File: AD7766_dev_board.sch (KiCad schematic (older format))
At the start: 62 parts, among them J1 Conn_Coaxial, J2 Conn_Coaxial, J3 Conn_01x06_Male, J4 Conn_01x10_Male, U1 PWR_JACK_POS, U2 PWR_JACK_GND, U3 ADR445, U4 ADP3330-5, U5 ADP3330-2.5, U6 ADP3330-2.5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

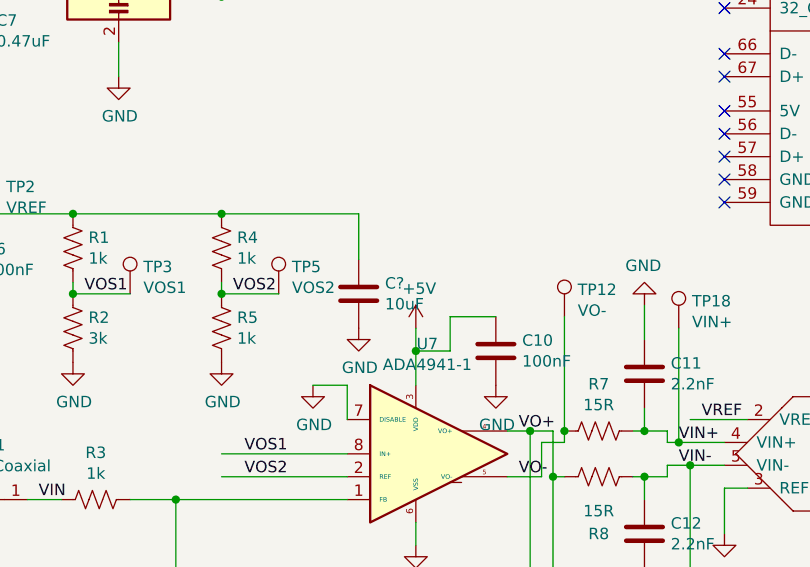
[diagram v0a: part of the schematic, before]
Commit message: revised README, fixed bill of materials
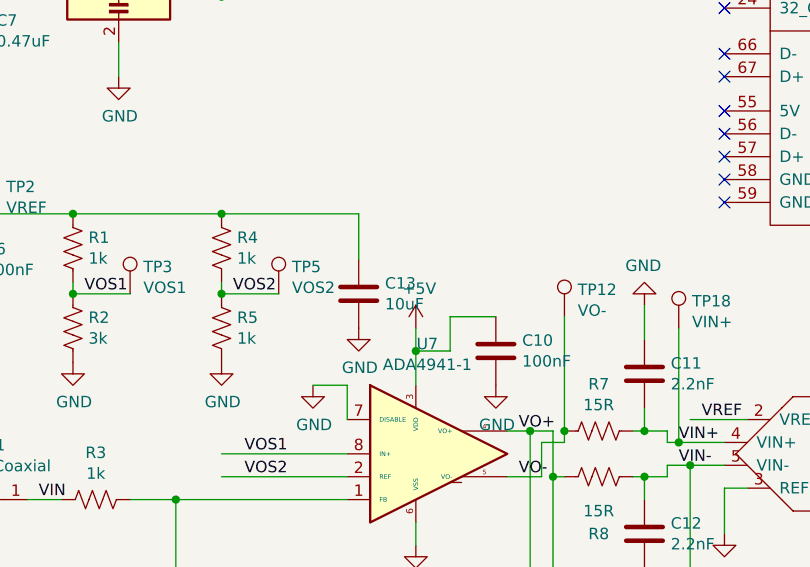
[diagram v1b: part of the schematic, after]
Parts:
- C13: renamed from C?; footprint (none) -> Capacitor_SMD:C_0805_2012Metric_Pad1.15x1.40mm_HandSolder
- D1: footprint Diode_SMD:D_0805_2012Metric_Pad1.15x1.40mm_HandSolder -> Diode_SMD:D_SMA-SMB_Universal_Handsoldering
- D2: Distributor (none) -> Digikey; Distributor Link (none) -> https://www.digikey.com/en/products/detail/nexperia-usa-inc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
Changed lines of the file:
@@
 F 0 "D1" H 2300 5915 50  0000 C CNN
 F 1 "DIODE" H 2300 5824 50  0000 C CNN
-F 2 "Diode_SMD:D_0805_2012Metric_Pad1.15x1.40mm_HandSolder" H 2300 5650 50  0001 C CNN
+F 2 "Diode_SMD:D_SMA-SMB_Universal_Handsoldering" H 2300 5650 50  0001 C CNN
 F 3 "~" H 2300 5650 50  0001 C CNN
 	1    2300 5650
@@
 F 2 "Package_TO_SOT_SMD:SC-59_Handsoldering" H 2850 6250 50  0001 C CNN
 F 3 "~" H 2850 6250 50  0001 C CNN
+F 4 "https://www.digikey.com/en/products/detail/nexperia-usa-inc/PESD15VL2BT215/1157421?s=N4IgTCBcDaIAoFEDKARAjAVgGoBkwCEAVEAXQF8g" H 2850 6250 50  0001 C CNN "Distributor Link"
+F 5 "Digikey" H 2850 6250 50  0001 C CNN "Distributor"
 	1    2850 6250
 	1    0    0    -1
@@
 VIN
 $Comp
-L Device:C C?
+L Device:C C13
 U 1 1 5FFE5A2E
 P 5050 4600
-F 0 "C?" H 5165 4646 50  0000 L CNN
+F 0 "C13" H 5165 4646 50  0000 L CNN
 F 1 "10uF" H 5165 4555 50  0000 L CNN
-F 2 "" H 5088 4450 50  0001 C CNN
+F 2 "Capacitor_SMD:C_0805_2012Metric_Pad1.15x1.40mm_HandSolder" H 5088 4450 50  0001 C CNN
 F 3 "~" H 5050 4600 50  0001 C CNN
 	1    5050 4600
@@
 Connection ~ 4450 4250
 $Comp
-L power:GND #PWR?
+L power:GND #PWR048
 U 1 1 5FFF02BA
 P 5050 4750
-F 0 "#PWR?" H 5050 4500 50  0001 C CNN
+F 0 "#PWR048" H 5050 4500 50  0001 C CNN
 F 1 "GND" H 5055 4577 50  0000 C CNN
 F 2 "" H 5050 4750 50  0001 C CNN

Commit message: updated with errors found in version 1, sending out version 2 for fabrication
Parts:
- removed C13: 10uF, Capacitor_SMD:C_0805_2012Metric_Pad1.15x1.40mm_HandSolder, symbol Device:C
- added H1, H2, H3, H4: MountingHole, my_library_foot:m3_mounting_hole, symbol Mechanical:MountingHole
- R1: value 1k -> 3k
- R2: value 3k -> 1k
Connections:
- wire segments 172 -> 170
- no-connect marks 48 -> 52
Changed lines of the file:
@@
 Wire Wire Line
 	2250 2350 2600 2350
-$Comp
-L power:GND #PWR010
-U 1 1 5F772035
-P 1950 4450
-F 0 "#PWR010" H 1950 4200 50  0001 C CNN
-F 1 "GND" H 1955 4277 50  0000 C CNN
-F 2 "" H 1950 4450 50  0001 C CNN
-F 3 "" H 1950 4450 50  0001 C CNN
-	1    1950 4450
-	1    0    0    -1
-$EndComp
 Wire Wire Line
 	1950 4450 1950 4250
@@
 P 3800 4400
 F 0 "R1" H 3868 4446 50  0000 L CNN
-F 1 "1k" H 3868 4355 50  0000 L CNN
+F 1 "3k" H 3868 4355 50  0000 L CNN
 F 2 "Resistor_SMD:R_0805_2012Metric_Pad1.15x1.40mm_HandSolder" V 3840 4390 50  0001 C CNN
 F 3 "~" H 3800 4400 50  0001 C CNN
@@
 P 3800 4750
 F 0 "R2" H 3868 4796 50  0000 L CNN
-F 1 "3k" H 3868 4705 50  0000 L CNN
+F 1 "1k" H 3868 4705 50  0000 L CNN
 F 2 "Resistor_SMD:R_0805_2012Metric_Pad1.15x1.40mm_HandSolder" V 3840 4740 50  0001 C CNN
 F 3 "~" H 3800 4750 50  0001 C CNN
@@
 Text Label 2850 5800 0    50   ~ 0
 VIN
-$Comp
-L Device:C C13
-U 1 1 5FFE5A2E
-P 5050 4600
-F 0 "C13" H 5165 4646 50  0000 L CNN
-F 1 "10uF" H 5165 4555 50  0000 L CNN
-F 2 "Capacitor_SMD:C_0805_2012Metric_Pad1.15x1.40mm_HandSolder" H 5088 4450 50  0001 C CNN
-F 3 "~" H 5050 4600 50  0001 C CNN
-	1    5050 4600
-	1    0    0    -1
-$EndComp
-Wire Wire Line
-	4450 4250 5050 4250
-Wire Wire Line
-	5050 4250 5050 4450
-Connection ~ 4450 4250
-$Comp
-L power:GND #PWR048
-U 1 1 5FFF02BA
-P 5050 4750
-F 0 "#PWR048" H 5050 4500 50  0001 C CNN
-F 1 "GND" H 5055 4577 50  0000 C CNN
-F 2 "" H 5050 4750 50  0001 C CNN
-F 3 "" H 5050 4750 50  0001 C CNN
-	1    5050 4750
-	1    0    0    -1
-$EndComp
+NoConn ~ 1950 4450
+NoConn ~ 5600 4050
+NoConn ~ 5700 4400
+NoConn ~ 5150 5500
+$Comp
+L Mechanical:MountingHole H1
+U 1 1 5F936B39
+P 1400 6750
+F 0 "H1" H 1500 6796 50  0000 L CNN
+F 1 "MountingHole" H 1500 6705 50  0000 L CNN
+F 2 "my_library_foot:m3_mounting_hole" H 1400 6750 50  0001 C CNN
+F 3 "~" H 1400 6750 50  0001 C CNN
+	1    1400 6750
+	1    0    0    -1
+$EndComp
+$Comp
+L Mechanical:MountingHole H2
+U 1 1 5F9376EF
+P 1450 7000
+F 0 "H2" H 1550 7046 50  0000 L CNN
+F 1 "MountingHole" H 1550 6955 50  0000 L CNN
+F 2 "my_library_foot:m3_mounting_hole" H 1450 7000 50  0001 C CNN
+F 3 "~" H 1450 7000 50  0001 C CNN
+	1    1450 7000
+	1    0    0    -1
+$EndComp
+$Comp
+L Mechanical:MountingHole H3
+U 1 1 5F937926
+P 1450 7200
+F 0 "H3" H 1550 7246 50  0000 L CNN
+F 1 "MountingHole" H 1550 7155 50  0000 L CNN
+F 2 "my_library_foot:m3_mounting_hole" H 1450 7200 50  0001 C CNN
+F 3 "~" H 1450 7200 50  0001 C CNN
+	1    1450 7200
+	1    0    0    -1
+$EndComp
+$Comp
+L Mechanical:MountingHole H4
+U 1 1 5F937B08
+P 2300 7050
+F 0 "H4" H 2400 7096 50  0000 L CNN
+F 1 "MountingHole" H 2400 7005 50  0000 L CNN
+F 2 "my_library_foot:m3_mounting_hole" H 2300 7050 50  0001 C CNN
+F 3 "~" H 2300 7050 50  0001 C CNN
+	1    2300 7050
+	1    0    0    -1
+$EndComp

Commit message: added allPCB BOM and position files. Hopefully it works.
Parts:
- C1: Manufacturer Part # (none) -> GRM21BR6YA106ME43L
- C10, C3, C6, CD1, CD4, CD6: Manufacturer Part # (none) -> C0805C104M5RACTU
- C11, C12: Manufacturer Part # (none) -> CL21B222KDCNFNC
- C2, C4, C5, C7, C8, C9: Manufacturer Part # (none) -> 08051C474K4Z2A
- CD2, CD5, CD8: Manufacturer Part # (none) -> 08055C102KAT2A
- CD3, CD7, CD9: Manufacturer Part # (none) -> C0805C101J5GACTU
- D1: Manufacturer Part # (none) -> SK220ATR
- D2: Manufacturer Part # (none) -> PESD15VL2BT,215
- FL1, FL2, FL3: Manufacturer Part # (none) -> NFL21SP157X1C3D
- R1: Manufacturer Part # (none) -> CRG0805F3K0
- R10: Manufacturer Part # (none) -> RR1220P-241-D
- R2, R3, R4, R5, R6: Manufacturer Part # (none) -> RC0805FR-071KL
- R7, R8: Manufacturer Part # (none) -> RK73H2ATTD15R0F
- R9: Manufacturer Part # (none) -> CRGCQ0805F120R
- U3: Manufacturer Part # (none) -> ADR445ARZ
- U4: Manufacturer Part # (none) -> ADP3330ARTZ-5-RL7
- U5, U6: Manufacturer Part # (none) -> ADP3330ARTZ-2.5-R7
- U7: Manufacturer Part # (none) -> ADA4941-1YRZ
- U8: Manufacturer Part # (none) -> AD7766BRUZ

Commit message: found issue of MCLK not being divided down to 2.5V, but remaining at 3.3V. Fixed issue on PCB, added to README
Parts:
- added R?: 320, symbol Device:R_US
- added R?: 1k, symbol Device:R_US
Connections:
- wire segments 170 -> 174
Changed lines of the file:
@@
 Text Label 6400 1950 0    50   ~ 0
 DRDY
-Text Label 6400 1850 0    50   ~ 0
-MCLK
 NoConn ~ 6650 2150
 NoConn ~ 8850 1350
@@
 	1    0    0    -1
 $EndComp
+$Comp
+L Device:R_US R?
+U 1 1 5F9A459D
+P 5900 1850
+F 0 "R?" V 5695 1850 50  0000 C CNN
+F 1 "320" V 5786 1850 50  0000 C CNN
+F 2 "" V 5940 1840 50  0001 C CNN
+F 3 "~" H 5900 1850 50  0001 C CNN
+	1    5900 1850
+	0    1    1    0
+$EndComp
+$Comp
+L Device:R_US R?
+U 1 1 5F9A69D8
+P 5500 2150
+F 0 "R?" H 5432 2104 50  0000 R CNN
+F 1 "1k" H 5432 2195 50  0000 R CNN
+F 2 "" V 5540 2140 50  0001 C CNN
+F 3 "~" H 5500 2150 50  0001 C CNN
+	1    5500 2150
+	-1   0    0    1
+$EndComp
+Wire Wire Line
+	5500 2000 5500 1850
+Wire Wire Line
+	5500 1850 5750 1850
+Wire Wire Line
+	5500 2300 5500 2500
+$Comp
+L power:GND #PWR?
+U 1 1 5F9BA794
+P 5500 2500
+F 0 "#PWR?" H 5500 2250 50  0001 C CNN
+F 1 "GND" H 5505 2327 50  0000 C CNN
+F 2 "" H 5500 2500 50  0001 C CNN
+F 3 "" H 5500 2500 50  0001 C CNN
+	1    5500 2500
+	1    0    0    -1
+$EndComp
+Text Label 5100 1850 0    50   ~ 0
+MCLK
+Wire Wire Line
+	5500 1850 5050 1850
+Connection ~ 5500 1850
 $EndSCHEMATC
